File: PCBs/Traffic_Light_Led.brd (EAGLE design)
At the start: 33 x 28 mm, 10 parts

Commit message: Renamed files .
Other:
- outline, holes or cut-outs redrawn
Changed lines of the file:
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@@
 <drawing>
 <settings>
-<setting alwaysvectorfont="no"/>
+<setting alwaysvectorfont="yes"/>
 <setting verticaltext="up"/>
 </settings>
@@
 <board>
 <plain>
-<wire x1="0" y1="0" x2="33" y2="0" width="0" layer="20"/>
-<wire x1="33" y1="0" x2="33" y2="28" width="0" layer="20"/>
-<wire x1="33" y1="28" x2="0" y2="28" width="0" layer="20"/>
-<wire x1="0" y1="28" x2="0" y2="0" width="0" layer="20"/>
+<wire x1="0" y1="24.58579375" x2="0" y2="1" width="0" layer="20"/>
+<wire x1="0" y1="1" x2="1" y2="0" width="0" layer="20" curve="90"/>
+<wire x1="1" y1="0" x2="32" y2="0" width="0" layer="20"/>
+<wire x1="32" y1="0" x2="33" y2="1" width="0" layer="20" curve="90"/>
+<wire x1="33" y1="1" x2="33" y2="24.58579375" width="0" layer="20"/>
+<wire x1="33" y1="24.58579375" x2="29.58579375" y2="28" width="0" layer="20" curve="90"/>
+<wire x1="29.58579375" y1="28" x2="3.41420625" y2="28" width="0" layer="20"/>
+<wire x1="3.41420625" y1="28" x2="0" y2="24.58579375" width="0" layer="20" curve="90"/>
 </plain>
 <attributes>

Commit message: New Update
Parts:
- moved R1 1.57 mm to (26.9, 15.8)
- moved RED1 1.49 mm to (26.8, 7.07)
- moved RED 1.10 mm to (27.3, 24.1)
- moved GREEN1 0.95 mm to (19.3, 7.13)
- moved R2 0.66 mm to (20.3, 15.8)
- moved R3 0.66 mm to (12.3, 15.8)
- moved GREEN 0.51 mm to (20.2, 24.1)
- moved YELLOW1 0.42 mm to (11.8, 7.09)
- moved YELLOW 0.31 mm to (12.3, 24.2)
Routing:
- net GND: track 38.2 -> 36.8 mm
- net N$1: track 5.83 -> 5.10 mm
- net N$2: track 5.87 -> 5.23 mm
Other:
- board size 33 x 28 mm -> 37.5 x 27.5 mm
- board text added: "Pinwheel Robotics"
- board text added: "care@pinwheel.in"

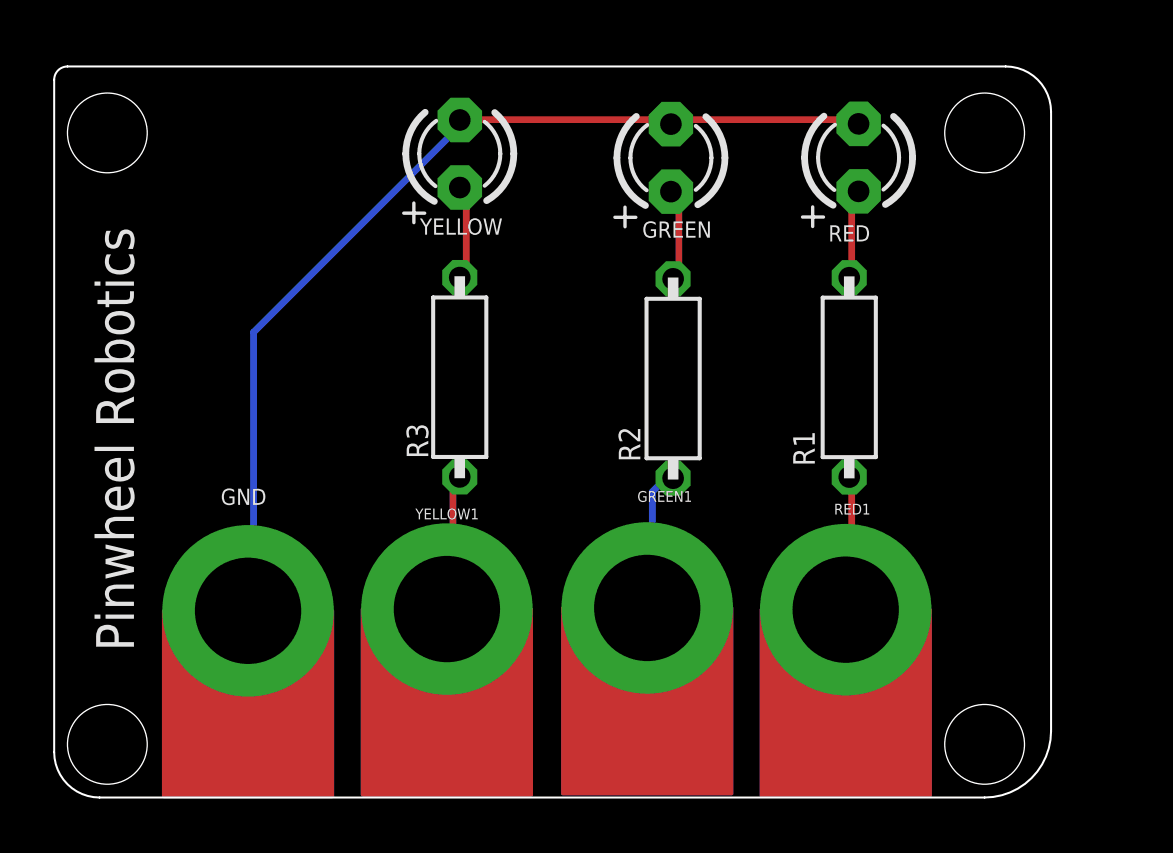
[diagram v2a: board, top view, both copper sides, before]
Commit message: New Update for board curv
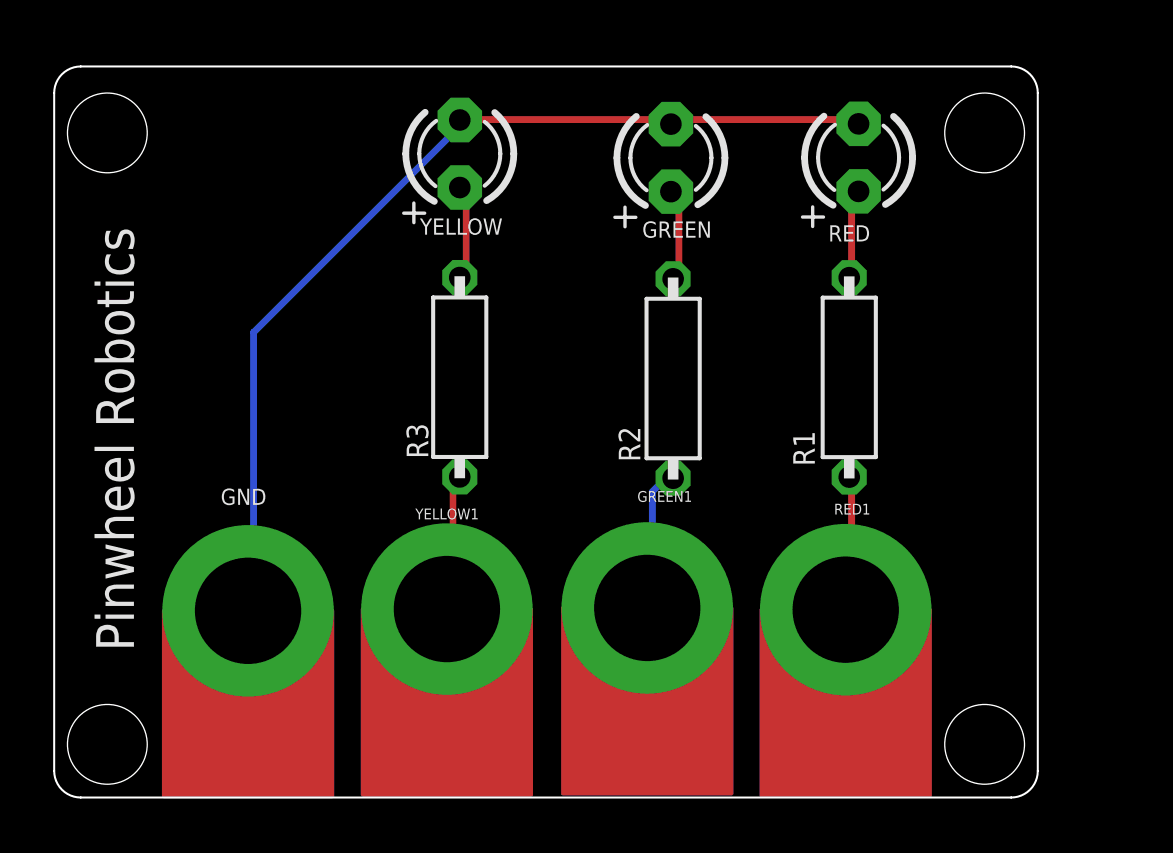
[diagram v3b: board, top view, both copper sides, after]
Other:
- board size 37.5 x 27.5 mm -> 37 x 27.5 mm
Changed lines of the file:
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@@
 <hole x="32" y="25" drill="3"/>
 <hole x="-1" y="25" drill="3"/>
-<wire x1="32" y1="0" x2="-1.292896875" y2="0" width="0.0762" layer="20"/>
-<wire x1="-1.292896875" y1="0" x2="-3" y2="1.707103125" width="0.0762" layer="20" curve="-90"/>
-<wire x1="-3" y1="1.707103125" x2="-3" y2="27" width="0.0762" layer="20"/>
-<wire x1="-3" y1="27" x2="-2.5" y2="27.5" width="0.0762" layer="20" curve="-90"/>
-<wire x1="-2.5" y1="27.5" x2="32.792896875" y2="27.5" width="0.0762" layer="20"/>
-<wire x1="32.792896875" y1="27.5" x2="34.5" y2="25.792896875" width="0.0762" layer="20" curve="-90"/>
-<wire x1="34.5" y1="25.792896875" x2="34.5" y2="2.5" width="0.0762" layer="20"/>
-<wire x1="34.5" y1="2.5" x2="32" y2="0" width="0.0762" layer="20" curve="-90"/>
+<wire x1="-2" y1="27.5" x2="33" y2="27.5" width="0.0762" layer="20"/>
+<wire x1="33" y1="27.5" x2="34" y2="26.5" width="0.0762" layer="20" curve="-90"/>
+<wire x1="34" y1="26.5" x2="34" y2="1" width="0.0762" layer="20"/>
+<wire x1="34" y1="1" x2="33" y2="0" width="0.0762" layer="20" curve="-90"/>
+<wire x1="33" y1="0" x2="-2" y2="0" width="0.0762" layer="20"/>
+<wire x1="-2" y1="0" x2="-3" y2="1" width="0.0762" layer="20" curve="-90"/>
+<wire x1="-3" y1="1" x2="-3" y2="26.5" width="0.0762" layer="20"/>
+<wire x1="-3" y1="26.5" x2="-2" y2="27.5" width="0.0762" layer="20" curve="-90"/>
 <text x="0" y="5.5" size="1.4224" layer="21" rot="R90">Pinwheel Robotics</text>
 <text x="24" y="14.5" size="1.4224" layer="22" rot="MR0">care@pinwheel.in</text>

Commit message: Dimension added
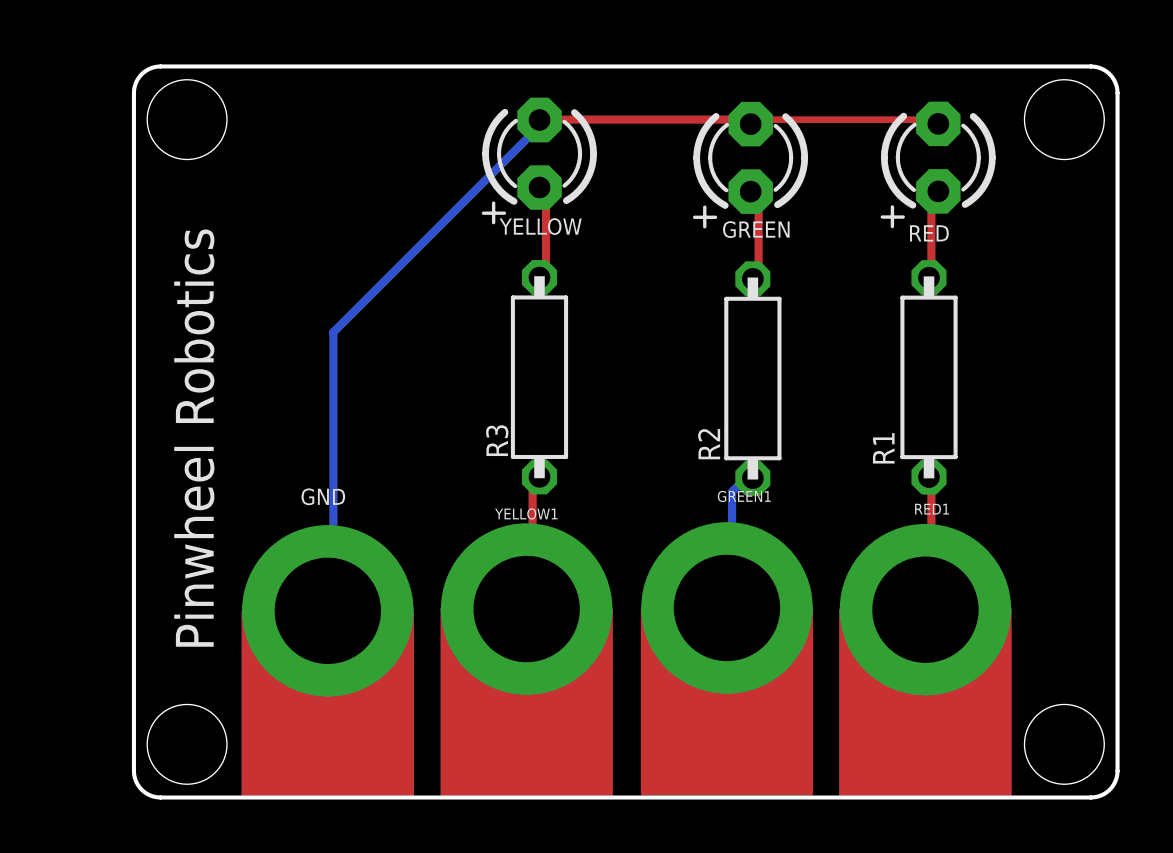
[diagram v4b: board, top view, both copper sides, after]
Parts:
- moved GND 3.00 mm to (7.29, 7.02)
- moved GREEN 3.00 mm to (23.2, 24.1)
- moved GREEN1 3.00 mm to (22.3, 7.13)
- moved R1 3.00 mm to (29.9, 15.8)
- moved R2 3.00 mm to (23.3, 15.8)
- moved R3 3.00 mm to (15.3, 15.8)
- moved RED 3.00 mm to (30.3, 24.1)
- moved RED1 3.00 mm to (29.8, 7.07)
- moved YELLOW 3.00 mm to (15.3, 24.2)
- moved YELLOW1 3.00 mm to (14.8, 7.09)
